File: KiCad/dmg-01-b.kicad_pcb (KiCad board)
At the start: 2 copper layers, 83 x 78.5 mm, 64 parts, among them CN1 SCREEN, CN2 CART, CN3 EXT, CN4 AUDIO, CN5 POWER, CN6 BATTERY, P1 GND PAD, P2 GND PAD, P3 GND PAD, P4 GND PAD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

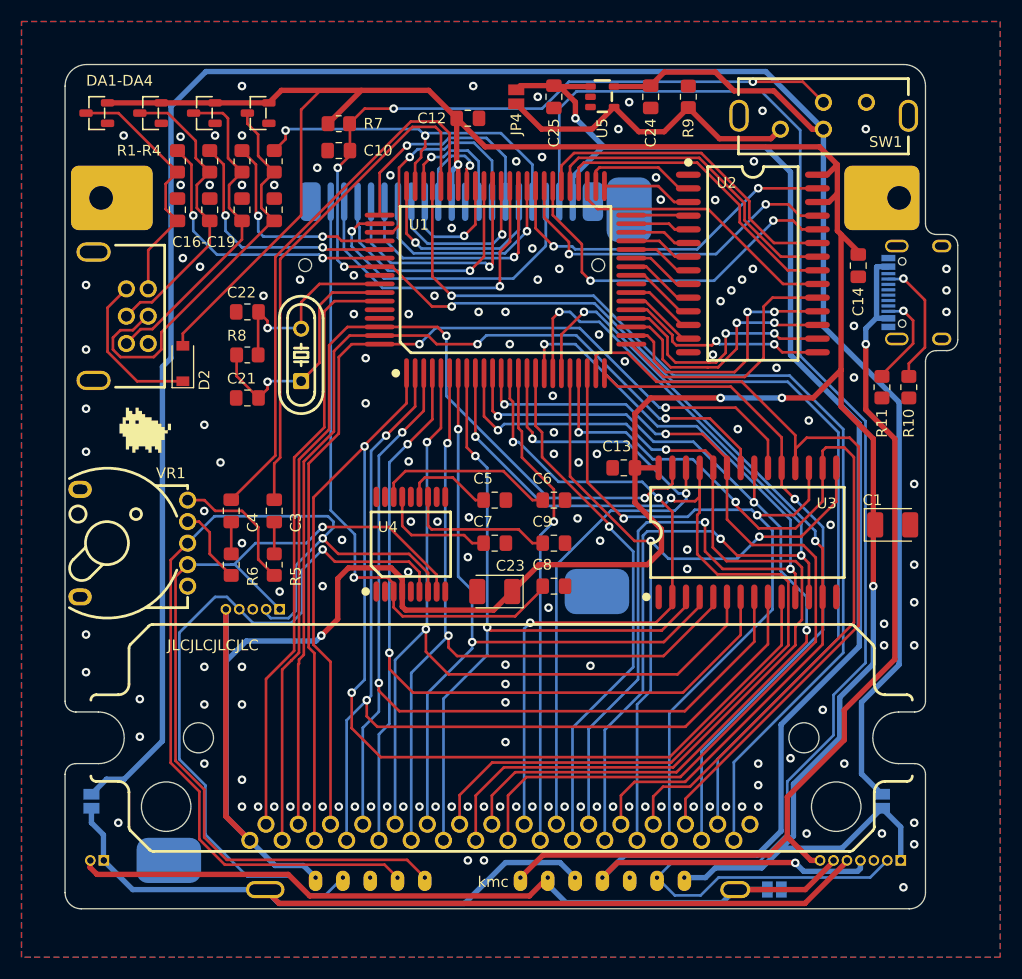
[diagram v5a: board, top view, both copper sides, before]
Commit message: test connectors (for history, to be removed)
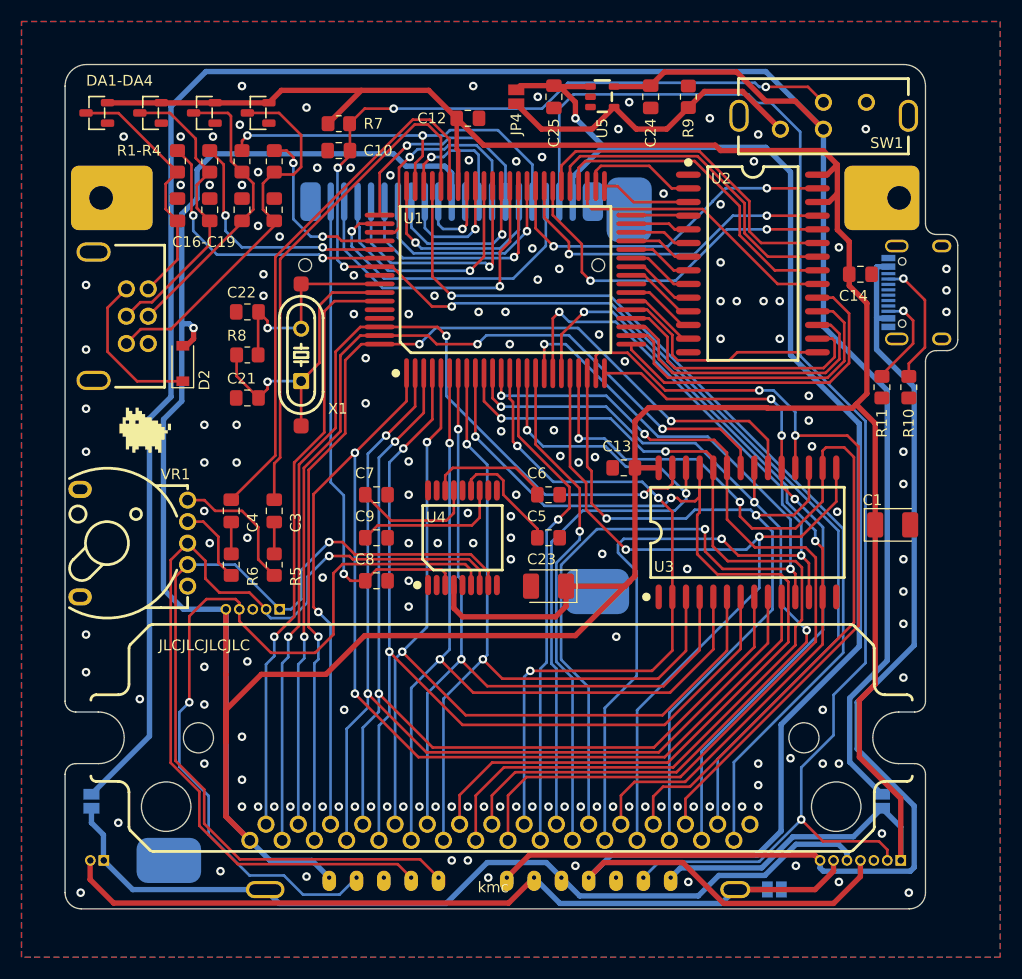
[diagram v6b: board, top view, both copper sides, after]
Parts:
- CN1: footprint kmc_lib:DMG_FPC_CONN -> dmg_lib:DMG_FPC_CONN
- CN2: footprint kmc_lib:DMG_CART_CONN -> dmg_lib:DMG_CART_CONN
- CN3: footprint kmc_lib:DMG_LINK_CONN -> dmg_lib:DMG_LINK_CONN
- H1: footprint kmc_lib:DMG_BATTERY_PADS -> dmg_lib:DMG_BATTERY_PADS
- JP1: value bypass -> BAT SWITCH
- JP2: value bypass -> 5V SWITCH
- JP3: value bypass -> GND -BATT
- P1: value GND PAD -> CART SHIELD GND PADS; footprint kmc_lib:DMG_CART_SHIELD_CONTACT -> dmg_lib:DMG_CART_SHIELD_CONTACT
- P2, P3, P4: footprint kmc_lib:DMG_GROUNDPAD -> dmg_lib:DMG_GROUNDPAD
- SW1: footprint kmc_lib:DMG_POWER_SWITCH -> dmg_lib:DMG_POWER_SWITCH
- U1: footprint kmc_lib:DMG_CPU -> dmg_lib:DMG_CPU
- U2, U3: footprint kmc_lib:DMG_RAM_64K -> dmg_lib:DMG_RAM_64K
- U4: footprint kmc_lib:SSOP-18_6X7.4MM_P0.8MM -> dmg_lib:DMG_AMP
- VR1: footprint kmc_lib:RES-TH_RK10J12E002L -> dmg_lib:DMG_VOLUME_POT
- X1: footprint kmc_lib:HC-49S -> dmg_lib:HC-49S
- moved C8 16.5 mm to (59.0, 74.0)
- moved C9 16.5 mm to (59.0, 70.0)
- moved C7 11.9 mm to (59.0, 66.0)
- moved C5 6.10 mm to (75.0, 70.0)
- moved C23 5.02 mm to (75.0, 74.5)
- moved DA1 5.00 mm to (43.0, 30.5)
- moved DA2 5.00 mm to (48.0, 30.5)
- moved U4 4.84 mm to (67.0, 70.0)
- moved C16 3.00 mm to (46.5, 39.5)
- moved C17 3.00 mm to (49.5, 39.5)
- moved R1 3.00 mm to (46.5, 35.0)
- moved R2 3.00 mm to (49.5, 35.0)
- moved H2 1.27 mm to (78.7, 96.5)
- moved H3 1.27 mm to (59.7, 101.6)
- moved C14 0.82 mm to (104.0, 45.5), turned to 180 degrees
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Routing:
- net +5V: track 357.4 -> 420.1 mm, vias 5 -> 1
- net +BATT: track 109.2 -> 82.0 mm
- net VCC: track 91.2 -> 103.8 mm, vias 1 -> 0
- net VEE: track 141.4 -> 129.1 mm, vias 0 -> 1
- net /EXT_SD: track 38.5 -> 27.0 mm
- net /SPKR: track 56.6 -> 46.5 mm
- net /AMP_EN: track 68.0 -> 76.8 mm
- net /MD7: track 24.4 -> 31.0 mm
- net Net-(C6-Pad1): track 16.7 -> 11.1 mm
- net +VSW: track 150.2 -> 155.7 mm, vias 2 -> 1
- net /RST: track 152.5 -> 147.1 mm
- net /SND: track 94.9 -> 89.5 mm
- net /A6: track 66.7 -> 72.1 mm
- net /A7: track 65.5 -> 70.8 mm
- net /MD6: track 24.6 -> 29.7 mm, vias 2 -> 0
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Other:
- board text added: "v1.4"
- board text removed: "v1.3.1"

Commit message: fixed battery connector (!) less stupid routing in some areas minor changes
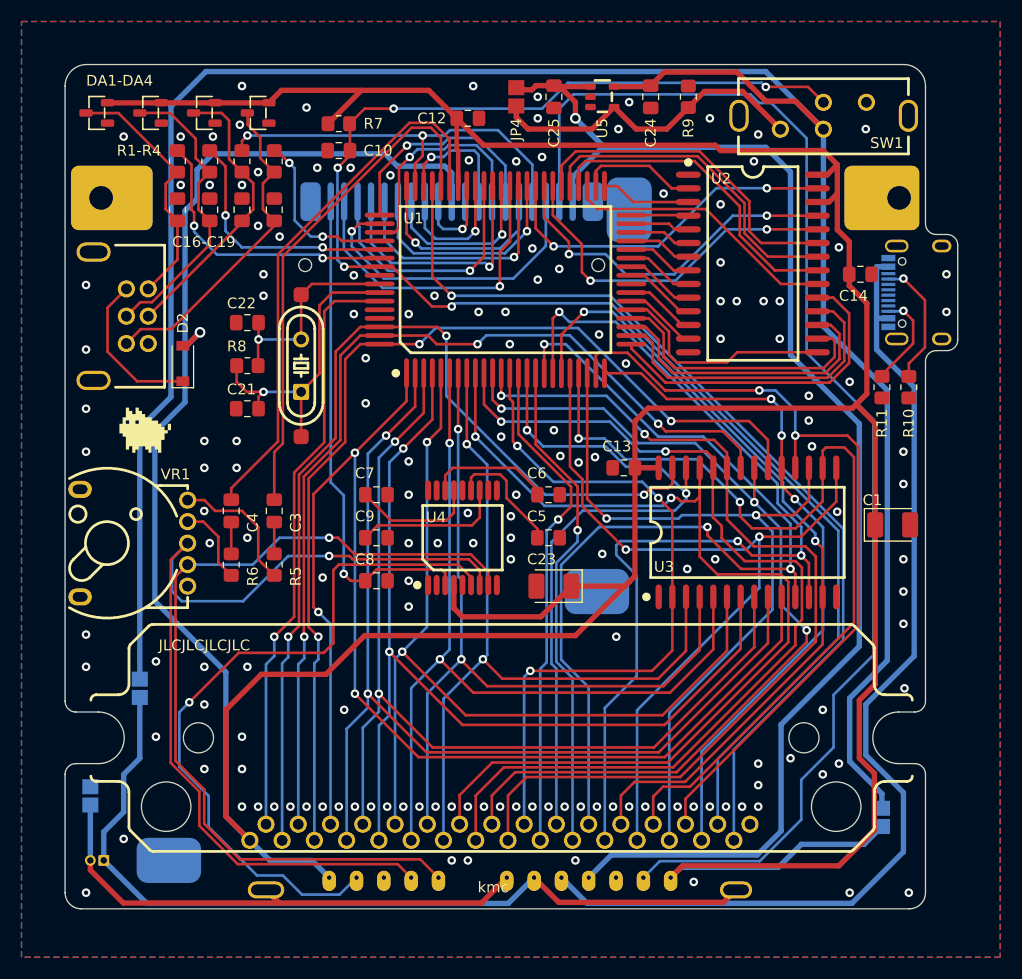
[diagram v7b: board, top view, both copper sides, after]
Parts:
- removed the CN4 at (47.5, 76.7)
- removed CN5: POWER, easyeda2kicad:CONN-TH_7P-P1.25_HCTL_HC-1.25-7AW
- H1: footprint dmg_lib:DMG_BATTERY_PADS -> kmc_lib:DMG_BATTERY_PADS
- moved JP1 64.2 mm to (32.4, 94.0), turned to 90 degrees
- moved JP2 11.4 mm to (37.0, 84.0)
- moved JP3 1.50 mm to (106.0, 96.0)
- moved C21 1.00 mm to (47.0, 58.0)
- moved C22 1.00 mm to (47.0, 50.0)
- moved R8 1.00 mm to (47.0, 54.0)
- moved X1 1.00 mm to (52.0, 54.0)
- moved C23 0.50 mm to (75.5, 74.5)
- moved H1 0.08 mm to (70.6, 102.6)
- renumbered CN6 to CN4, JP3 to JP1, JP1 to JP2, JP2 to JP3
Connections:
- H1 pad 1: -BATT -> +BATT
- H1 pad 2: +BATT -> -BATT
- H2 pad 5: +BATT -> VCC
- H2 pad 6: -BATT -> +BATT
- H2 pad 7: VCC -> -BATT
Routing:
- net -BATT: track 79.0 -> 48.8 mm
- net +VSW: track 155.7 -> 125.7 mm
- net VIN: track 220.3 -> 209.1 mm
- net /AMP_EN: track 76.8 -> 66.1 mm
- net VEE: track 129.1 -> 119.5 mm, vias 1 -> 0
- net VCC: track 103.8 -> 96.1 mm
- net /EXT_CLK: track 35.1 -> 30.2 mm
- net /LPOT: track 85.7 -> 81.1 mm
- net +5V: track 420.1 -> 416.2 mm
- net +BATT: track 82.0 -> 79.4 mm
- net /MA8: track 31.9 -> 33.4 mm
- net /D0: track 90.3 -> 89.5 mm
- net /CK1: track 27.8 -> 28.6 mm
- net /SCK: track 16.6 -> 15.9 mm
- net /RPOT: track 86.7 -> 87.5 mm
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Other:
- board text added: "+"
- board text added: "-"
